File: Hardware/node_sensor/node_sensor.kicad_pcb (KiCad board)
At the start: 2 copper layers, 50 x 50 mm, 14 parts, among them J1 Conn_Jack-DC, J2 Pump, J3 Light, U1 DevKitESP32, U2 DHT11, U3 BH1750, U4 ADS1115, U5 DS3231, U6 Soil-Moisture, U7 Soil-Moisture, U8 Soil-Moisture, U9 Soil-Moisture

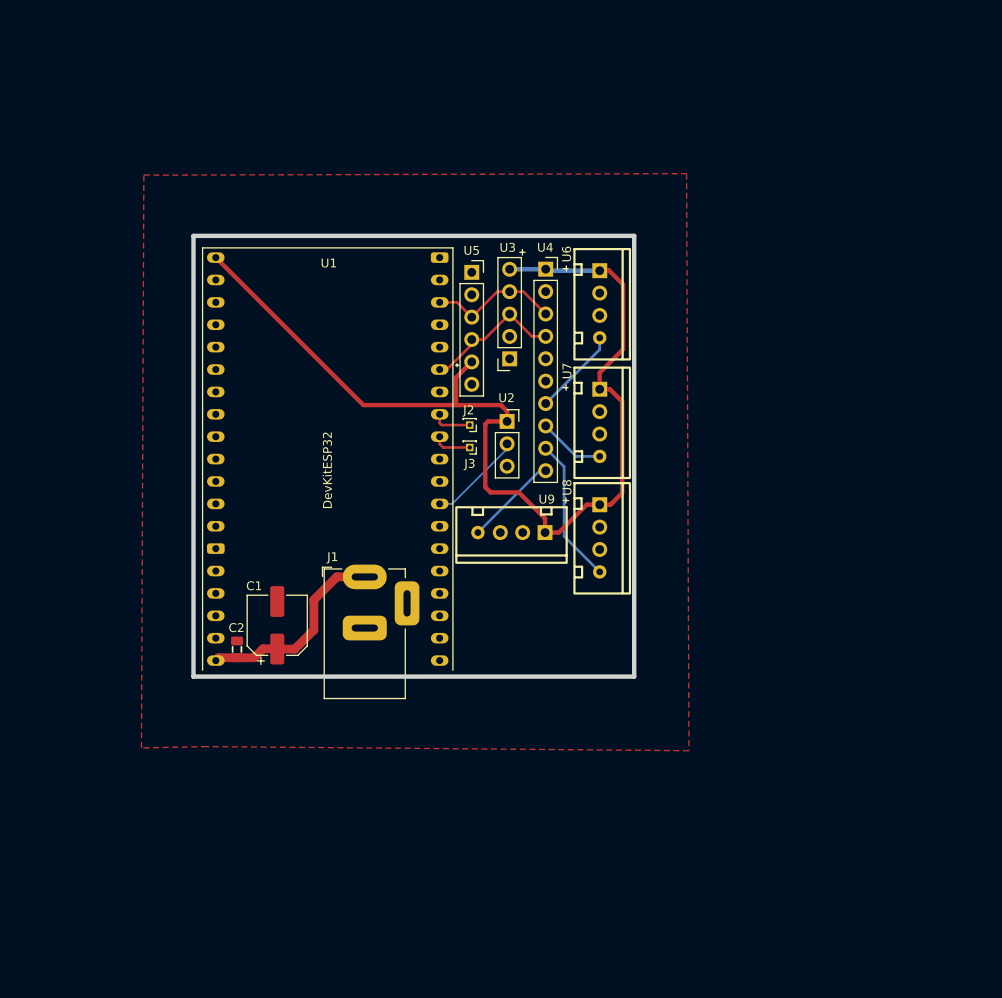
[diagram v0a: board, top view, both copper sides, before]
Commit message: change topic - switch pi 4
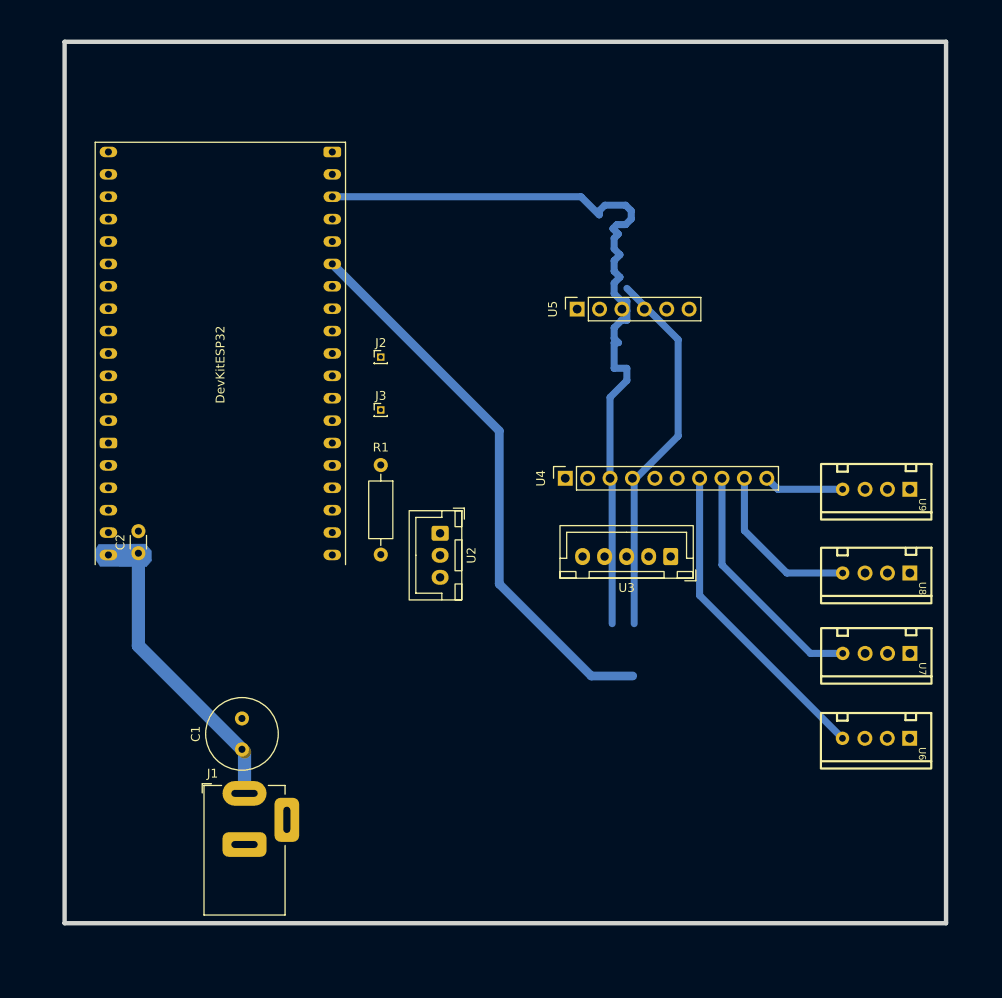
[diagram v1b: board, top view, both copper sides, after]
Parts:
- added R1: 10K, Resistor_THT:R_Axial_DIN0207_L6.3mm_D2.5mm_P10.16mm_Horizontal, F.Cu at (111.2, 66.0)
- C1: footprint MY_FOOTPRINTS:CP_Elec_6.3x7.7 -> Capacitor_THT:C_Radial_D8.0mm_H11.5mm_P3.50mm
- C2: footprint MY_FOOTPRINTS:C_0805 -> Capacitor_THT:C_Disc_D3.0mm_W1.6mm_P2.50mm
- U2: footprint Connector_PinSocket_2.54mm:PinSocket_1x03_P2.54mm_Vertical -> Connector_JST:JST_XH_B3B-XH-A_1x03_P2.50mm_Vertical
- U3: footprint Connector_PinSocket_2.54mm:PinSocket_1x05_P2.54mm_Vertical -> Connector_JST:JST_XH_B5B-XH-A_1x05_P2.50mm_Vertical
- moved U6 58.4 mm to (167.4, 97.0), turned to -90 degrees
- moved U9 41.7 mm to (167.5, 68.8)
- moved U7 40.9 mm to (167.5, 87.4), turned to -90 degrees
- moved U8 31.6 mm to (167.5, 78.2), turned to -90 degrees
- moved U3 28.9 mm to (144.1, 76.4)
- moved J1 28.1 mm to (95.8, 103.2)
- moved U4 23.8 mm to (132.2, 67.5), turned to 90 degrees
- moved U1 17.1 mm to (80.3, 30.5)
- moved C2 15.6 mm to (83.8, 76.0)
- moved U2 14.8 mm to (118.0, 73.7), turned to -90 degrees
- moved C1 14.6 mm to (95.5, 98.2)
- moved J2 12.7 mm to (111.2, 53.8), turned to 0 degrees
- moved U5 12.7 mm to (133.5, 48.3), turned to 90 degrees
- moved J3 11.0 mm to (111.2, 59.8), turned to 0 degrees
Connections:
- U1 pad 14: unconnected-(U1-GND-Pad14) -> GND
- U1 pad 18: GND -> unconnected-(U1-CMD-Pad18)
- U1 pad 38: unconnected-(U1-GND-Pad38) -> GND
- U2 pad 2: /1_wire -> Net-(U2-D0)
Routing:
- net +3V3: track 117.8 -> 0.06 mm
- net /I2C_SDA: track 16.0 -> 106.1 mm
- net /I2C_SCL: track 15.0 -> 90.5 mm
- net Net-(U4-A0): track 9.99 -> 36.2 mm
- net Net-(U4-A1): track 7.56 -> 27.7 mm
- net /1_wire: track 10.8 -> 0.00 mm
- net +5V: track 22.9 -> 32.2 mm
- net Net-(J2-Pin_1): track 4.49 -> 0.00 mm
- net Net-(J3-Pin_1): track 4.40 -> 0.00 mm
- net Net-(U4-A2): track 17.0 -> 19.1 mm
- net Net-(U4-A3): track 10.6 -> 9.13 mm
- removed copper zone on F.Cu, net GND
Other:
- board size 50 x 50 mm -> 100 x 100 mm

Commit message: updated pcb
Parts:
- added REF**: MountingHole_3.2mm_M3, MountingHole:MountingHole_3.2mm_M3, F.Cu at (79.3, 114.1)
- added REF**: MountingHole_3.2mm_M3, MountingHole:MountingHole_3.2mm_M3, F.Cu at (171.3, 114.1)
- added REF**: MountingHole_3.2mm_M3, MountingHole:MountingHole_3.2mm_M3, F.Cu at (171.3, 22.1)
- added REF**: MountingHole_3.2mm_M3, MountingHole:MountingHole_3.2mm_M3, F.Cu at (79.3, 22.1)
- moved U5 11.7 mm to (144.9, 45.6), turned to -90 degrees
- moved U4 7.53 mm to (131.6, 75.0)
- moved U6 7.53 mm to (166.9, 104.5)
- moved U8 7.53 mm to (166.9, 85.8)
- moved U9 7.53 mm to (166.9, 76.3)
- moved U3 7.53 mm to (143.6, 83.9)
- moved U7 7.53 mm to (166.9, 94.9)
- moved J3 2.00 mm to (113.2, 59.5)
- moved J2 1.97 mm to (113.2, 53.7)
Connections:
- U1 pad 32: unconnected-(U1-GND-Pad32) -> GND
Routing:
- net +3V3: track 0.06 -> 257.7 mm
- net /I2C_SDA: track 106.1 -> 74.7 mm, vias 0 -> 2
- net Net-(J3-Pin_1): track 0.00 -> 13.0 mm
- net Net-(J2-Pin_1): track 0.00 -> 11.4 mm
- net /1_wire: track 0.00 -> 11.3 mm
- net /I2C_SCL: track 90.5 -> 80.2 mm
- net Net-(U2-D0): track 0.00 -> 6.65 mm
- net GND: vias 0 -> 4
- added copper zone on B.Cu, net GND

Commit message: fusion-sensor,check nvs-DB
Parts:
- moved R1 13.5 mm to (112.0, 79.5), turned to 90 degrees
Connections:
- R1 pad 2: Net-(U2-D0) -> +3V3
- U2 pad 2: Net-(U2-D0) -> /1_wire
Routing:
- net /1_wire: track 11.3 -> 32.4 mm
- net +3V3: track 257.7 -> 267.4 mm
- net Net-(U2-D0): track 6.65 -> 0.00 mm
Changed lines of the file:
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@@
 	(footprint "Resistor_THT:R_Axial_DIN0207_L6.3mm_D2.5mm_P10.16mm_Horizontal"
 		(layer "F.Cu")
-		(at 111.25 66 -90)
+		(at 112.03 79.45 90)
 		(descr "Resistor, Axial_DIN0207 series, Axial, Horizontal, pin pitch=10.16mm, 0.25W = 1/4W, length*diameter=6.3*2.5mm^2, http://cdn-reichelt.de/documents/datenblatt/B400/1_4W%23YAG.pdf")
 		(tags "Resistor Axial_DIN0207 series Axial Horizontal pin pitch 10.16mm 0.25W = 1/4W length 6.3mm diameter 2.5mm")
 		(property "Reference" "R1"
-			(at -2 0 180)
+			(at -2 0 0)
 			(layer "F.SilkS")
 			(effects
@@
 		(duplicate_pad_numbers_are_jumpers no)
 		(fp_line
-			(start 1.04 0)
-			(end 1.81 0)
+			(start 9.12 0)
+			(end 8.35 0)
 			(stroke
 				(width 0.12)
@@
 		)
 		(fp_line
-			(start 9.12 0)
-			(end 8.35 0)
+			(start 1.04 0)
+			(end 1.81 0)
 			(stroke
 				(width 0.12)
@@
 		)
 		(fp_line
-			(start 0 0)
-			(end 1.93 0)
+			(start 10.16 0)
+			(end 8.23 0)
 			(stroke
 				(width 0.1)
@@
 		)
 		(fp_line
-			(start 10.16 0)
-			(end 8.23 0)
+			(start 0 0)
+			(end 1.93 0)
 			(stroke
 				(width 0.1)
@@
 		)
 		(pad "1" thru_hole circle
-			(at 0 0 270)
+			(at 0 0 90)
 			(size 1.6 1.6)
 			(drill 0.8)
@@
 		)
 		(pad "2" thru_hole circle
-			(at 10.16 0 270)
+			(at 10.16 0 90)
 			(size 1.6 1.6)
 			(drill 0.8)
 			(layers "*.Cu" "*.Mask")
 			(remove_unused_layers no)
-			(net "Net-(U2-D0)")
+			(net "+3V3")
 			(pintype "passive")
 		)
@@
 				(font
 					(size 0.8 0.8)
-					(thickness 0.3)
+					(thickness 0.2)
 				)
 			)
@@
 			)
 		)
+		(model "${KICAD_OWNER_3D}/Connector/XH_2.54/Thru Vertical/JST - XH - Thru (V) - 4Pin - 2.54mm.stp"
+			(offset
+				(xyz 0 0 0)
+			)
+			(scale
+				(xyz 1 1 1)
+			)
+			(rotate
+				(xyz -0 -0 90)
+			)
+		)
 	)
 	(footprint "Capacitor_THT:C_Disc_D3.0mm_W1.6mm_P2.50mm"
@@
 			(layers "*.Cu" "*.Mask")
 			(remove_unused_layers no)
-			(net "Net-(U2-D0)")
+			(net "/1_wire")
 			(pinfunction "D0_2")
 			(pintype "output")
@@
 				(font
 					(size 0.8 0.8)
-					(thickness 0.3)
+					(thickness 0.2)
 				)
 			)
@@
 			)
 		)
-		(property "Description" ""
+		(property "Description" "Generic connector, single row, 01x04, script generated (kicad-library-utils/schlib/autogen/connector/)"
 			(at 0 0 270)
 			(unlocked yes)
@@
 		(sheetname "/")
 		(sheetfile "node_sensor.kicad_sch")
-		(units
-			(unit
-				(name "A")
-				(pins "1" "2" "3" "4")
-			)
-		)
 		(attr through_hole)
 		(duplicate_pad_numbers_are_jumpers no)
@@
 			)
 		)
+		(model "${KICAD_OWNER_3D}/Connector/XH_2.54/Thru Vertical/JST - XH - Thru (V) - 4Pin - 2.54mm.stp"
+			(offset
+				(xyz 0 0 0)
+			)
+			(scale
+				(xyz 1 1 1)
+			)
+			(rotate
+				(xyz -0 -0 90)
+			)
+		)
 	)
 	(footprint "MY_FOOTPRINTS:BarrelJack_Horizontal"
@@
 		(tags "Power Jack")
 		(property "Reference" "J1"
-			(at 2.26 -3.6325 180)
+			(at 2.425 -3.95 180)
 			(layer "F.SilkS")
 			(effects
@@
 			)
 		)
-		(property "Description" "DC Barrel Jack"
+		(property "Description" ""
 			(at 0 0 90)
 			(unlocked yes)
@@
 		(sheetname "/")
 		(sheetfile "node_sensor.kicad_sch")
-		(units
-			(unit
-				(name "A")
-				(pins "3" "1" "2")
-			)
-		)
 		(attr through_hole)
 		(duplicate_pad_numbers_are_jumpers no)
@@
 			)
 		)
+		(model "${KICAD_OWNER_3D}/Connector/Jack_DC/DC Power Jack 5.5mm x 2.1mm.STEP"
+			(offset
+				(xyz -10.5 0.5 6.5)
+			)
+			(scale
+				(xyz 1 1 1)
+			)
+			(rotate
+				(xyz -90 -0 90)
+			)
+		)
 	)
 	(footprint "MY_FOOTPRINTS:Conn_XH-P2.54mm-4P"
@@
 				(font
 					(size 0.8 0.8)
-					(thickness 0.3)
+					(thickness 0.2)
 				)
 			)
@@
 			)
 		)
-		(property "Description" ""
+		(property "Description" "Generic connector, single row, 01x04, script generated (kicad-library-utils/schlib/autogen/connector/)"
 			(at 0 0 270)
 			(unlocked yes)
@@
 		(sheetname "/")
 		(sheetfile "node_sensor.kicad_sch")
-		(units
-			(unit
-				(name "A")
-				(pins "1" "2" "3" "4")
-			)
-		)
 		(attr through_hole)
 		(duplicate_pad_numbers_are_jumpers no)
@@
 			)
 		)
+		(model "${KICAD_OWNER_3D}/Connector/XH_2.54/Thru Vertical/JST - XH - Thru (V) - 4Pin - 2.54mm.stp"
+			(offset
+				(xyz 0 0 0)
+			)
+			(scale
+				(xyz 1 1 1)
+			)
+			(rotate
+				(xyz -0 -0 90)
+			)
+		)
 	)
 	(footprint "MountingHole:MountingHole_3.2mm_M3"
@@
 				(font
 					(size 0.8 0.8)
-					(thickness 0.3)
+					(thickness 0.2)
 				)
 			)
@@
 			)
 		)
-		(property "Description" ""
+		(property "Description" "Generic connector, single row, 01x04, script generated (kicad-library-utils/schlib/autogen/connector/)"
 			(at 0 0 270)
 			(unlocked yes)
@@
 		(sheetname "/")
 		(sheetfile "node_sensor.kicad_sch")
-		(units
-			(unit
-				(name "A")
-				(pins "1" "2" "3" "4")
-			)
-		)
 		(attr through_hole)
 		(duplicate_pad_numbers_are_jumpers no)
@@
 			)
 		)
+		(model "${KICAD_OWNER_3D}/Connector/XH_2.54/Thru Vertical/JST - XH - Thru (V) - 4Pin - 2.54mm.stp"
+			(offset
+				(xyz 0 0 0)
+			)
+			(scale
+				(xyz 1 1 1)
+			)
+			(rotate
+				(xyz -0 -0 90)
+			)
+		)
 	)
 	(footprint "Connector_PinSocket_2.54mm:PinSocket_1x10_P2.54mm_Vertical"
@@
 	)
 	(segment
-		(start 111.25 66)
-		(end 111.25 61.4)
+		(start 117.98 76.24)
+		(end 115.24 76.24)
 		(width 0.8)
 		(layer "B.Cu")
@@
 	)
 	(segment
-		(start 111.25 61.4)
+		(start 115.24 76.24)
+		(end 112.03 79.45)
+		(width 0.8)
+		(layer "B.Cu")
+		(net "/1_wire")
+	)
+	(segment
+		(start 108.9 59.05)
 		(end 108.27 58.42)
 		(width 0.8)
@@
 	)
 	(segment
-		(start 108.27 58.42)
-		(end 105.75 58.42)
+		(start 112.03 79.45)
+		(end 108.9 76.32)
 		(width 0.8)
 		(layer "B.Cu")
@@
 	)
 	(segment
-		(start 111.25 76.16)
-		(end 117.9 76.16)
+		(start 108.9 76.32)
+		(end 108.9 59.05)
 		(width 0.8)
 		(layer "B.Cu")
-		(net "Net-(U2-D0)")
+		(net "/1_wire")
+	)
+	(segment
+		(start 108.27 58.42)
+		(end 105.75 58.42)
+		(width 0.8)
+		(layer "B.Cu")
+		(net "/1_wire")
 	)
 	(segment
@@
 	)
 	(segment
+		(start 117.98 70.5)
+		(end 117.98 73.74)
+		(width 0.8)
+		(layer "B.Cu")
+		(net "+3V3")
+	)
+	(segment
 		(start 100.77 47.94)
 		(end 83.31 30.48)
@@
 	)
 	(segment
+		(start 112.03 69.29)
+		(end 116.77 69.29)
+		(width 0.8)
+		(layer "B.Cu")
+		(net "+3V3")
+	)
+	(segment
 		(start 131.63 81.93)
 		(end 131.63 75.01)
@@
 	)
 	(segment
+		(start 116.77 69.29)
+		(end 117.98 70.5)
+		(width 0.8)
+		(layer "B.Cu")
+		(net "+3V3")
+	)
+	(segment
 		(start 134.72 60.84)
 		(end 134.72 67.8)
@@
 		)
 		(min_thickness 0.25)
-		(fill yes
+		(fill
 			(thermal_gap 0.5)
 			(thermal_bridge_width 0.5)
